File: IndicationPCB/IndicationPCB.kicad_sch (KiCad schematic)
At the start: 0 parts

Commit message: Draft
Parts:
- added D1, D2, D3, D4, D5: LTST-C235KGKRKT, LED_SMD:LED_LiteOn_LTST-C235KGKRKT, symbol LED:LTST-C235KGKRKT
- added J1: Conn_01x03, Connector_Molex:Molex_Nano-Fit_105309-xx03_1x03_P2.50mm_Vertical, symbol Connector_Generic:Conn_01x03
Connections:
- net +5V: now also D1.1 (K2), D2.1 (K2), D3.1 (K2), D4.1 (K2), D5.1 (K2), J1.1 (Pin_1)
- new net: D2.4 (K1), D3.2 (A2)
- new net: D3.4 (K1), D4.2 (A2)
- new net: D4.4 (K1), D5.2 (A2)
- new net: D1.4 (K1), D2.2 (A2)
- new net: D1.2 (A2), J1.2 (Pin_2)
- new net GNDPWR: D1.3 (A1), D2.3 (A1), D3.3 (A1), D4.3 (A1), D5.3 (A1), J1.3 (Pin_3)
- no-connect marks 0 -> 1
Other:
- note removed: "connector thing"
- note removed: "help me aaaahaahahah"

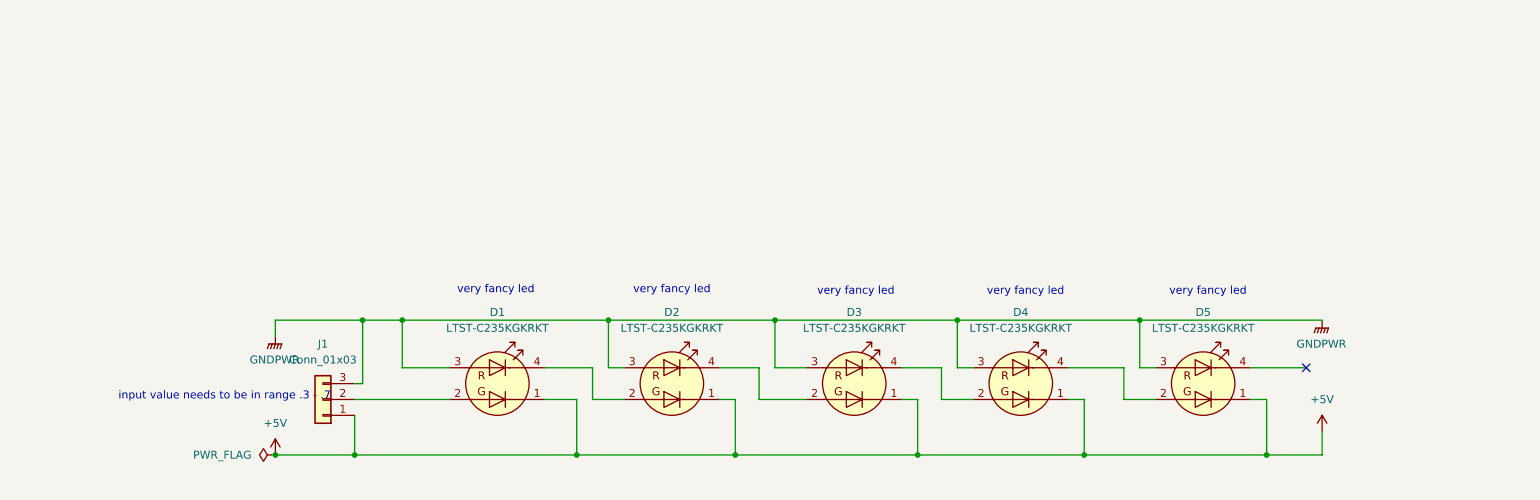
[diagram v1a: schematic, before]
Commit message: correct LEDS
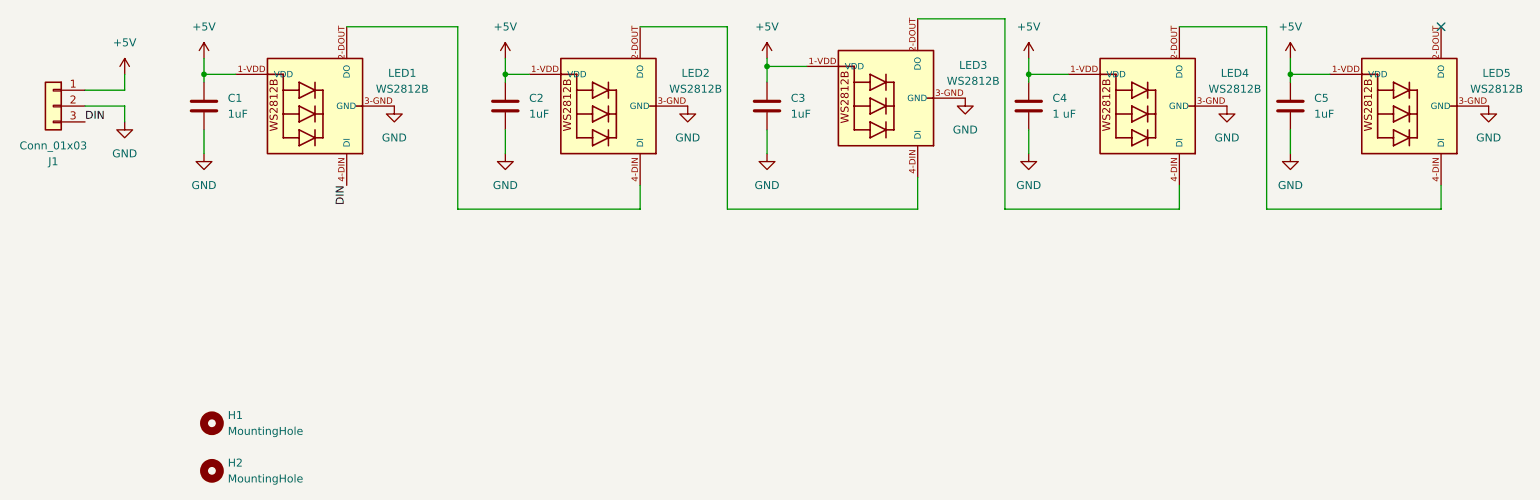
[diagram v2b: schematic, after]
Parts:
- removed D1, D2, D3, D4, D5: LTST-C235KGKRKT, LED_SMD:LED_LiteOn_LTST-C235KGKRKT, symbol LED:LTST-C235KGKRKT
- added C1, C2, C3, C5: 1uF, Capacitor_SMD:C_0603_1608Metric_Pad1.08x0.95mm_HandSolder, symbol Device:C
- added C4: 1 uF, Capacitor_SMD:C_0603_1608Metric_Pad1.08x0.95mm_HandSolder, symbol Device:C
- added H1, H2: MountingHole, MountingHole:MountingHole_3.2mm_M3, symbol Mechanical:MountingHole
- added LED1, LED2, LED3, LED4, LED5: WS2812B, WS2812B:WS2812B, symbol WS2812B:WS2812B
- J1: footprint Connector_Molex:Molex_Nano-Fit_105309-xx03_1x03_P2.50mm_Vertical -> Connector_Molex:Molex_Nano-Fit_105313-xx03_1x03_P2.50mm_Horizontal
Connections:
- net +5V: now also C1.1, C2.1, C3.1, C4.1, C5.1, LED1.1-VDD (VDD), LED2.1-VDD (VDD), LED3.1-VDD (VDD), LED4.1-VDD (VDD), LED5.1-VDD (VDD)
- net GND: now reaches J1.2 (Pin_2)
- net GND: now also C1.2, C2.2, C3.2, C4.2, C5.2, LED1.3-GND (GND), LED2.3-GND (GND), LED3.3-GND (GND), LED4.3-GND (GND), LED5.3-GND (GND)
- net GNDPWR renamed DIN
- net DIN: now also LED1.4-DIN (DI)
- new net: LED3.2-DOUT (DO), LED4.4-DIN (DI)
- new net: LED2.2-DOUT (DO), LED3.4-DIN (DI)
- new net: LED4.2-DOUT (DO), LED5.4-DIN (DI)
- new net: LED1.2-DOUT (DO), LED2.4-DIN (DI)
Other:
- note removed: "input value needs to be in range .3 - .7"
- note removed: "very fancy led"
- moved on the sheet: J1

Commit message: Added Models
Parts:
- added LOGO1: Dr. Hallock, UTSVT_Logos:UTSVT_Logo_Symbol, symbol utsvt_misc:Logo_Placeholder
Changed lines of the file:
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@@
+	)
+	(symbol
+		(lib_id "utsvt_misc:Logo_Placeholder")
+		(at 76.2 85.09 0)
+		(unit 1)
+		(exclude_from_sim no)
+		(in_bom yes)
+		(on_board yes)
+		(dnp no)
+		(fields_autoplaced yes)
+		(property "Reference" "LOGO1"
+			(at 76.2 81.28 0)
+			(effects
+				(font
+					(size 1.27 1.27)
+				)
+				(hide yes)
+			)
+		)
+		(property "Value" "Dr. Hallock"
+			(at 80.01 85.0899 0)
+			(effects
+				(font
+					(size 1.27 1.27)
+				)
+				(justify left)
+			)
+		)
+		(property "Footprint" "UTSVT_Logos:UTSVT_Logo_Symbol"
+			(at 76.2 83.185 0)
+			(effects
+				(font
+					(size 1.27 1.27)
+				)
+				(hide yes)
+			)
+		)
+		(property "Datasheet" ""
+			(at 76.2 83.185 0)
+			(effects
+				(font
+					(size 1.27 1.27)
+				)
+				(hide yes)
+			)
+		)
+		(property "Description" "Graph footprint placeholder"
+			(at 76.2 85.09 0)
+			(effects
+				(font
+					(size 1.27 1.27)
+				)
+				(hide yes)
+			)
+		)
+		(property "PN" ""
+			(at 76.2 85.09 0)
+			(effects
+				(font
+					(size 1.27 1.27)
+				)
+				(hide yes)
+			)
+		)
+		(property "p/n" ""
+			(at 76.2 85.09 0)
+			(effects
+				(font
+					(size 1.27 1.27)
+				)
+				(hide yes)
+			)
+		)
+		(instances
+			(project ""
+				(path "/8613a583-6d04-470b-b35c-aba3b37eb2c2"
+					(reference "LOGO1")
+					(unit 1)
+				)
+			)
+		)
 	)
 	(symbol

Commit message: logo!
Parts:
- LOGO1: footprint UTSVT_Logos:UTSVT_Logo_Symbol -> UTSVT_Logos:LHRs_LOGO
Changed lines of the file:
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@@
 			)
 		)
-		(property "Footprint" "UTSVT_Logos:UTSVT_Logo_Symbol"
+		(property "Footprint" "UTSVT_Logos:LHRs_LOGO"
 			(at 76.2 83.185 0)
 			(effects

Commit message: new connector
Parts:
- J1: footprint Connector_Molex:Molex_Nano-Fit_105313-xx03_1x03_P2.50mm_Horizontal -> Connector_Molex:Molex_Nano-Fit_105309-xx03_1x03_P2.50mm_Vertical
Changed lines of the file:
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@@
 			)
 		)
-		(property "Footprint" "Connector_Molex:Molex_Nano-Fit_105313-xx03_1x03_P2.50mm_Horizontal"
+		(property "Footprint" "Connector_Molex:Molex_Nano-Fit_105309-xx03_1x03_P2.50mm_Vertical"
 			(at 25.4 34.29 0)
 			(effects
